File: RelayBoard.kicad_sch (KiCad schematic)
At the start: 148 parts, among them J1 CONN_03-SCREW-5MM, J11 CONN_03-SCREW-5MM, J12 CONN_03-SCREW-5MM, J13 CONN_03-SCREW-5MM, J14 CONN_03-SCREW-5MM, J15 CONN_03-SCREW-5MM, J16 CONN_03-SCREW-5MM, J17 CONN_03-SCREW-5MM, J18 CONN_03-SCREW-5MM, J2 CONN_03-SCREW-5MM, J22 Conn_01x04, J24 Conn_01x06, J3 CONN_03-SCREW-5MM, J4 CONN_03-SCREW-5MM, J5 CONN_03-SCREW-5MM, J6 CONN_03-SCREW-5MM, J7 CONN_03-SCREW-5MM, J8 CONN_03-SCREW-5MM, K1 SANYOU_SRD_Form_C, K11 SANYOU_SRD_Form_C, K12 SANYOU_SRD_Form_C, K13 SANYOU_SRD_Form_C, K14 SANYOU_SRD_Form_C, K15 SANYOU_SRD_Form_C, K16 SANYOU_SRD_Form_C, K17 SANYOU_SRD_Form_C, K18 SANYOU_SRD_Form_C, K2 SANYOU_SRD_Form_C, K3 SANYOU_SRD_Form_C, K4 SANYOU_SRD_Form_C, K5 SANYOU_SRD_Form_C, K6 SANYOU_SRD_Form_C, K7 SANYOU_SRD_Form_C, K8 SANYOU_SRD_Form_C, Q1 ULN2803ADWR, Q2 ULN2803ADWR, U1 AP1117-33, U3 LTV-847, U4 LTV-847, U5 LTV-847, U6 LTV-847

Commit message: basic design with solid state relays complete
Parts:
- removed D11, D111, D112, D113, D114, D115, D116, D117, D118, D12, D13, D14, D15, D16, D17, D18: 1N4148W, Diode_SMD:D_SOD-123, symbol Diode:1N4148W
- removed K1, K11, K12, K13, K14, K15, K16, K17, K18, K2, K3, K4, K5, K6, K7, K8: SANYOU_SRD_Form_C, Relay_THT:Relay_SPDT_SANYOU_SRD_Series_Form_C, symbol Relay:SANYOU_SRD_Form_C
- removed R12, R13, R14, R15, R16, R17, R18, R19, R20, R21, R22, R23, R24, R25, R26, R27: 150, Resistor_SMD:R_0402_1005Metric, symbol Device:R
- removed U3, U4, U5, U6: LTV-847, digikey-footprints:DIP-16_W7.62mm, symbol dk_Optoisolators-Transistor-Photovoltaic-Output:LTV-847
- added U1, U11, U12, U13, U14, U15, U16, U17, U18, U2, U3, U4, U5, U6, U7, U8: (no value), symbol Relay_SolidState:TLP148G
- UP1: renamed from U1; value AP1117-33 -> (none); footprint Package_TO_SOT_SMD:SOT-223-3_TabPin2 -> (none)
- renumbered U2 to UM2
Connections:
- net LED1: now also UM2.5 (GPIO36)
- net LED2: now also UM2.8 (GPIO39)
- net LED3: now also UM2.10 (GPIO34)
- net LED4: now also UM2.11 (GPIO35)
- net at J1.3: now also U1.4
- net at D31.2 (A): now also U1.3
- net at J1.2: now also U1.5
- net at J1.1: now also U1.6
- net at R101.1: now also Q1.18 (OUT1), U1.1
- net at J11.1: now also U11.6
- net at J11.2: now also U11.5
- net at J11.3: now also U11.4
- net at D34.2 (A): now also U4.3
- net at R115.1: now also Q2.14 (OUT5), U15.1
- net at R114.1: now also Q2.15 (OUT4), U14.1
- net at R107.1: now also Q1.12 (OUT7), U7.1
- net at R104.1: now also Q1.16 (OUT3), U4.1
- net at R103.1: now also Q1.15 (OUT4), U3.1
- net at D37.2 (A): now also U7.3
- net at D32.2 (A): now also U2.3
- net at D315.2 (A): now also U15.3
- net at R117.1: now also Q2.12 (OUT7), U17.1
- net at D38.2 (A): now also U8.3
- net at J2.1: now also U2.6
- net at J2.2: now also U2.5
- net at J2.3: now also U2.4
- net at R112.1: now also Q2.17 (OUT2), U12.1
- net at Q2.11 (OUT8): now also R118.1, U18.1
- net at Q2.13 (OUT6): now also R116.1, U16.1
- net at Q2.16 (OUT3): now also R113.1, U13.1
- net at Q2.18 (OUT1): now also R111.1, U11.1
- net at D35.2 (A): now also U5.3
- net at D36.2 (A): now also U6.3
- net at R108.1: now also Q1.11 (OUT8), U8.1
- net at R102.1: now also Q1.17 (OUT2), U2.1
- net at R105.1: now also Q1.14 (OUT5), U5.1
- net at J17.3: now also U17.4
- net at D317.2 (A): now also U17.3
- net at J17.2: now also U17.5
- net at J17.1: now also U17.6
- net at R106.1: now also Q1.13 (OUT6), U6.1
- net at J4.3: now also U4.4
- net at J4.2: now also U4.5
- net at J4.1: now also U4.6
- net at J14.1: now also U14.6
- net at J14.2: now also U14.5
- net at J14.3: now also U14.4
- net at D314.2 (A): now also U14.3
- net at J12.1: now also U12.6
- net at J12.2: now also U12.5
- net at J12.3: now also U12.4
- net at D312.2 (A): now also U12.3
- net at D311.2 (A): now also U11.3
- net at J3.1: now also U3.6
- net at J3.2: now also U3.5
- net at J3.3: now also U3.4
- net at J5.3: now also U5.4
- net at J5.2: now also U5.5
- net at J5.1: now also U5.6
- net at J6.3: now also U6.4
- net at J6.2: now also U6.5
- net at J6.1: now also U6.6
- net at J13.1: now also U13.6
- net at J13.2: now also U13.5
- net at J13.3: now also U13.4
- net at D313.2 (A): now also U13.3
- net at J15.1: now also U15.6
- net at J15.2: now also U15.5
- net at J15.3: now also U15.4
- net at J18.1: now also U18.6
- net at J18.2: now also U18.5
- net at J18.3: now also U18.4
- net at J8.1: now also U8.6
- net at J8.2: now also U8.5
- net at J8.3: now also U8.4
- net at D33.2 (A): now also U3.3
- net at D316.2 (A): now also U16.3
- net at J7.1: now also U7.6
- net at J7.2: now also U7.5
- net at J7.3: now also U7.4
- net at J16.1: now also U16.6
- net at J16.2: now also U16.5
- net at J16.3: now also U16.4
- net at D318.2 (A): now also U18.3

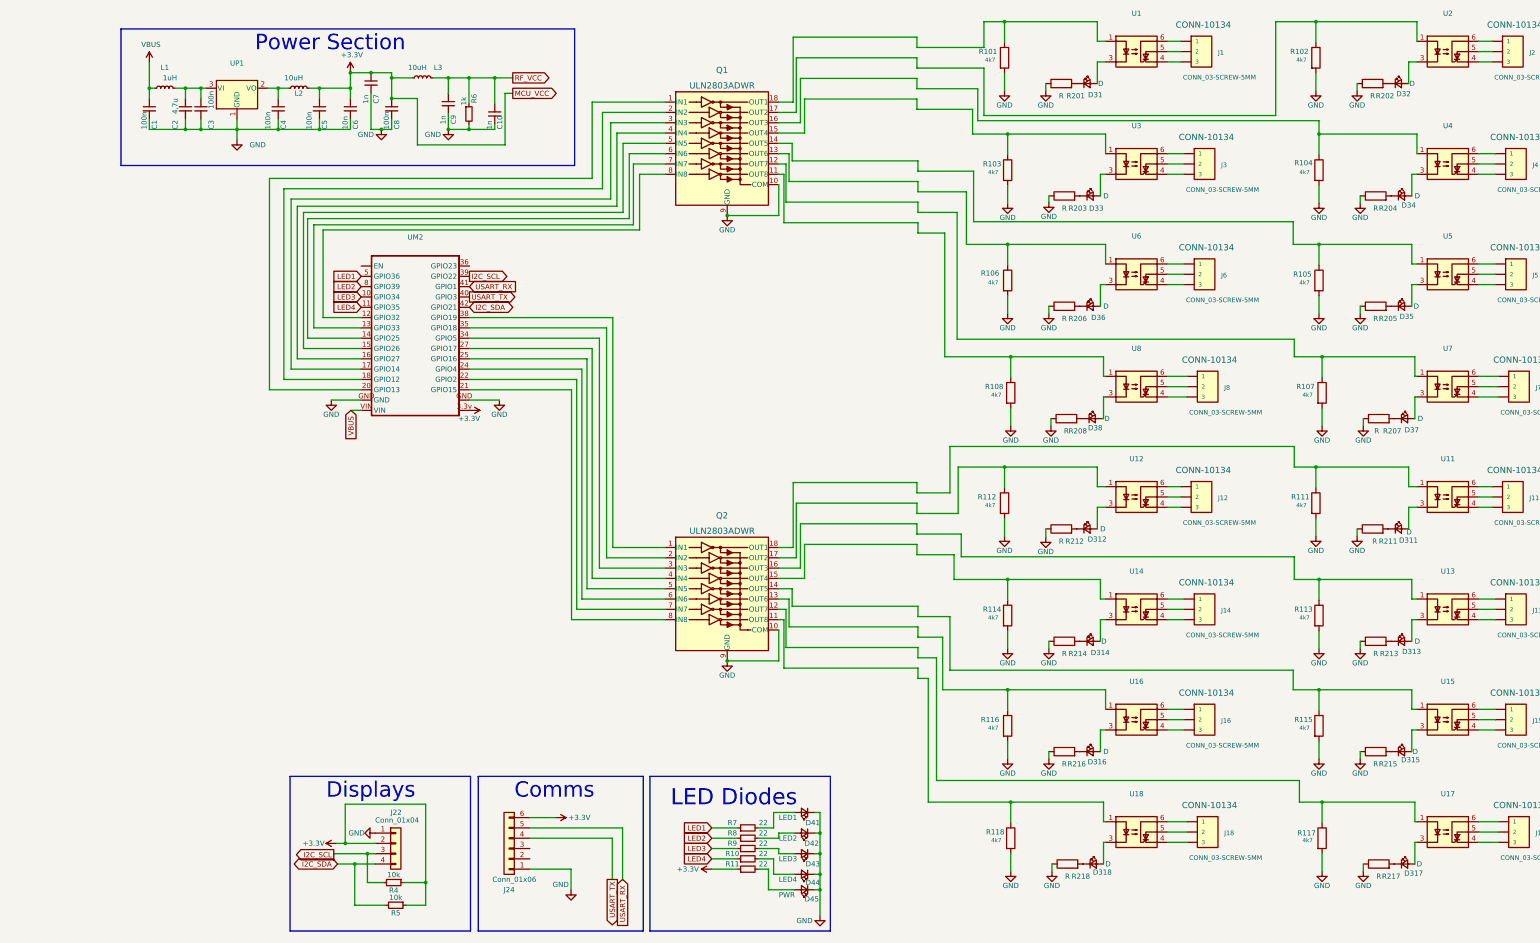
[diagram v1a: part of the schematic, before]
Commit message: remove esp32 and add Raspberry PI, along with AC power suppply
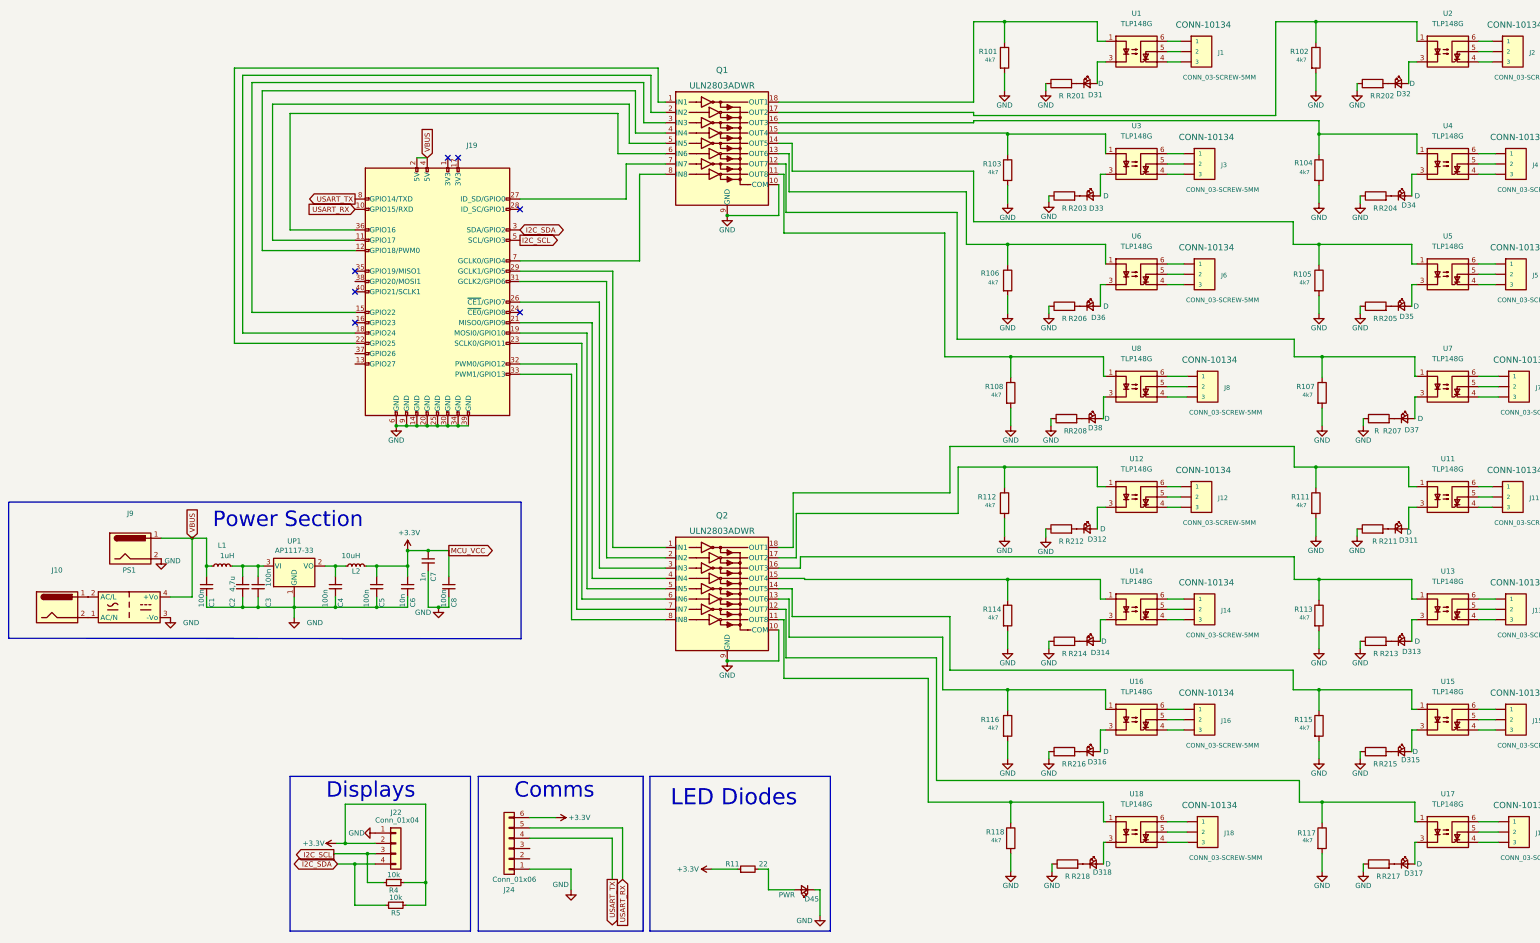
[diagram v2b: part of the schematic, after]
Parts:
- removed C10, C9: 1n, Capacitor_SMD:C_0603_1608Metric, symbol Device:C_Small
- removed D41: LED1, LED_SMD:LED_0402_1005Metric, symbol Device:LED_Small
- removed D42: LED2, LED_SMD:LED_0402_1005Metric, symbol Device:LED_Small
- removed D43: LED3, LED_SMD:LED_0402_1005Metric, symbol Device:LED_Small
- removed D44: LED4, LED_SMD:LED_0402_1005Metric, symbol Device:LED_Small
- removed L3: 10uH, Inductor_SMD:L_0805_2012Metric, symbol Device:L_Small
- removed R10, R7, R8, R9: 22, Resistor_SMD:R_0402_1005Metric, symbol Device:R_Small
- removed R6: 1k, Resistor_SMD:R_0805_2012Metric, symbol Device:R_Small
- removed UM2: (no value), symbol MCU_Espressif:NodeMCUDevKitV1
- added J10, J9: (no value), Connector_BarrelJack:BarrelJack_SwitchcraftConxall_RAPC10U_Horizontal, symbol Connector:Barrel_Jack
- added J19: (no value), symbol Connector:Raspberry_Pi_2_3
- added PS1: (no value), symbol Converter_ACDC:IRM-02-5
- U1, U11, U12, U13, U14, U15, U16, U17, U18, U2, U3, U4, U5, U6, U7, U8: value (none) -> TLP148G; footprint (none) -> Package_SO:MFSOP6-5_4.4x3.6mm_P1.27mm
- UP1: value (none) -> AP1117-33; footprint (none) -> Package_TO_SOT_SMD:SOT-223-3_TabPin2
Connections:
- net GND: now also J19.14 (GND), J19.20 (GND), J19.25 (GND), J19.30 (GND), J19.34 (GND), J19.39 (GND), J19.6 (GND), J19.9 (GND), J9.2, PS1.3 (-Vo)
- net I2C_SCL: now also J19.5 (SCL/GPIO3)
- net I2C_SDA: now also J19.3 (SDA/GPIO2)
- net USART_RX: now also J19.10 (GPIO15/RXD)
- net USART_TX: now also J19.8 (GPIO14/TXD)
- net VBUS: now also J19.2 (5V), J19.4 (5V), J9.1, PS1.4 (+Vo)
- net at Q2.1 (IN1): now also J19.29 (GCLK1/GPIO5)
- net at Q2.2 (IN2): now also J19.31 (GCLK2/GPIO6)
- net at Q2.3 (IN3): now also J19.26 (~{CE1}/GPIO7)
- net at Q2.4 (IN4): now also J19.21 (MISO0/GPIO9)
- net at Q2.5 (IN5): now also J19.19 (MOSI0/GPIO10)
- net at Q2.6 (IN6): now also J19.23 (SCLK0/GPIO11)
- net at Q2.7 (IN7): now also J19.32 (PWM0/GPIO12)
- net at Q2.8 (IN8): now also J19.33 (PWM1/GPIO13)
- net at Q1.8 (IN8): now also J19.7 (GCLK0/GPIO4)
- net at Q1.7 (IN7): now also J19.27 (ID_SD/GPIO0)
- net at Q1.6 (IN6): now also J19.36 (GPIO16)
- net at Q1.5 (IN5): now also J19.11 (GPIO17)
- net at Q1.4 (IN4): now also J19.12 (GPIO18/PWM0)
- net at Q1.3 (IN3): now also J19.15 (GPIO22)
- net at Q1.2 (IN2): now also J19.18 (GPIO24)
- net at Q1.1 (IN1): now also J19.22 (GPIO25)
- new net: J10.1, PS1.2 (AC/L)
- new net: J10.2, PS1.1 (AC/N)
- no-connect marks 0 -> 7
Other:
- moved on the sheet: C1, C2, C3, C4, C5, C6, C7, C8, L1, L2, UP1

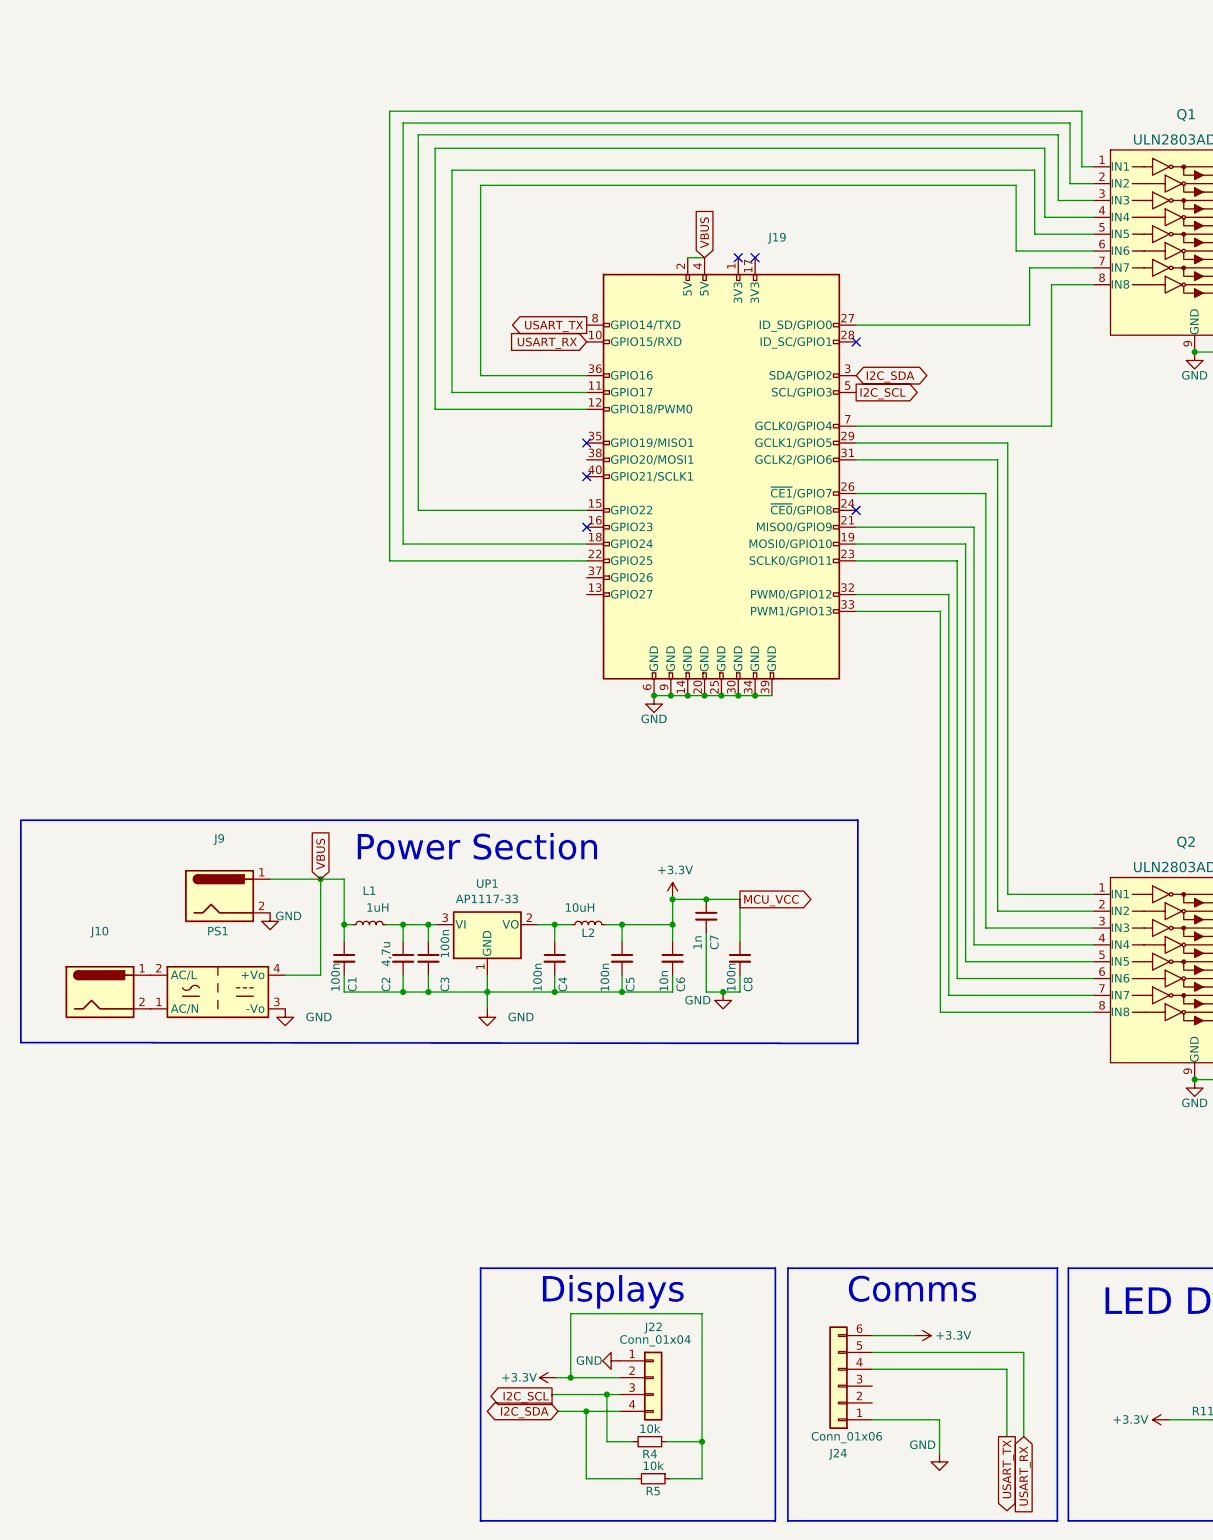
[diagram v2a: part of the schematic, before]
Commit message: replace connectors, reroute GPIOs and power
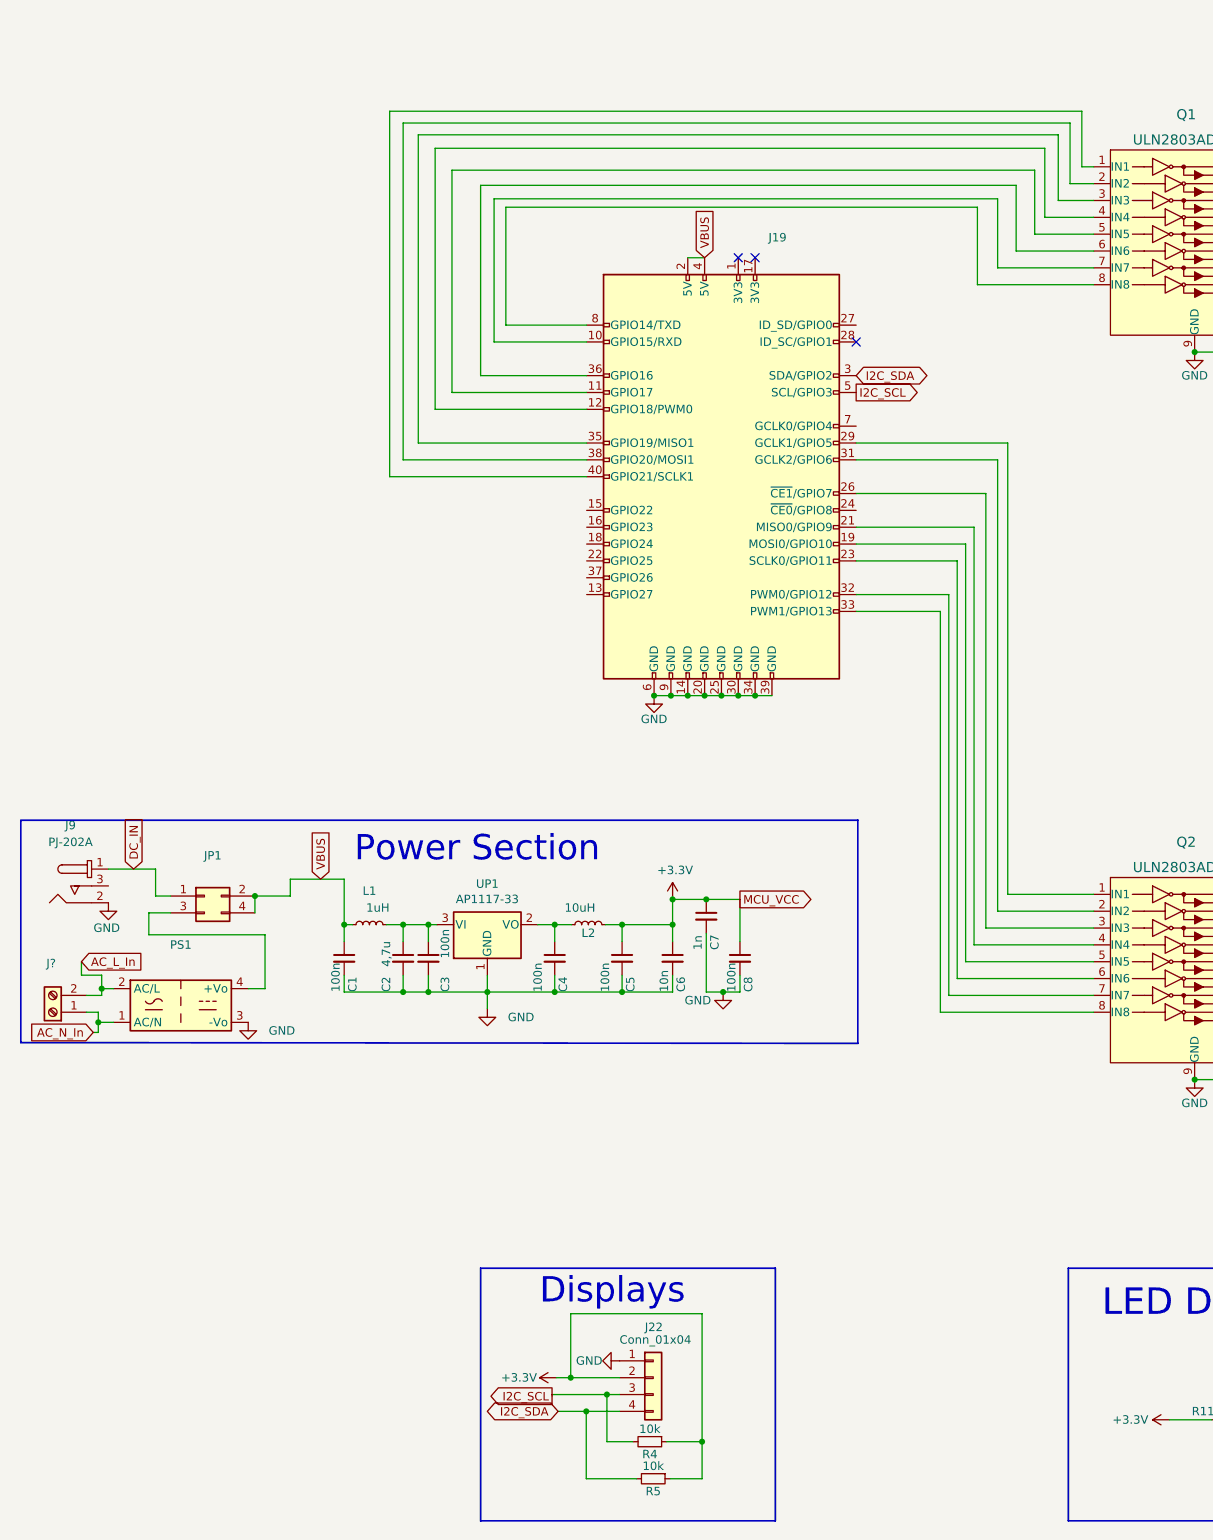
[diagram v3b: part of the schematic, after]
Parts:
- removed J10, J9: (no value), Connector_BarrelJack:BarrelJack_SwitchcraftConxall_RAPC10U_Horizontal, symbol Connector:Barrel_Jack
- removed J24: Conn_01x06, Connector_PinHeader_1.27mm:PinHeader_1x06_P1.27mm_Vertical, symbol Connector_Generic:Conn_01x06
- added J9: PJ-202A, Connectors:POWER_JACK_PTH_LOCK, symbol dk_Barrel-Power-Connectors:PJ-202A
- added J?: (no value), symbol Connector:Screw_Terminal_01x02
- added JP1: (no value), symbol Connector_Generic:Conn_02x02_Odd_Even
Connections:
- net USART_RX is gone; now on an unnamed net: J19.10 (GPIO15/RXD)
- net GND: now also J9.2
- net VBUS: now also JP1.2 (Pin_2), JP1.4 (Pin_4); no longer PS1.4 (+Vo)
- net at J19.15 (GPIO22): no longer Q1.3 (IN3)
- net at J19.18 (GPIO24): no longer Q1.2 (IN2)
- net at J19.22 (GPIO25): no longer Q1.1 (IN1)
- net at Q1.7 (IN7): no longer J19.27 (ID_SD/GPIO0)
- net at J19.35 (GPIO19/MISO1): now also Q1.3 (IN3)
- net at J19.38 (GPIO20/MOSI1): now also Q1.2 (IN2)
- net at J19.40 (GPIO21/SCLK1): now also Q1.1 (IN1)
- net at J19.7 (GCLK0/GPIO4): no longer Q1.8 (IN8)
- net AC_L_In: now reaches PS1.2 (AC/L)
- net AC_L_In: now also J?.2 (Pin_2)
- net AC_N_In: now reaches PS1.1 (AC/N)
- net AC_N_In: now also J?.1 (Pin_1)
- net USART_TX: no longer names the net of J19.8 (GPIO14/TXD)
- net USART_TX: now also Q1.8 (IN8)
- new net: JP1.3 (Pin_3), PS1.4 (+Vo)
- new net DC_IN: J9.1, JP1.1 (Pin_1)
- no-connect marks 7 -> 3
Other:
- note removed: "Comms"
- moved on the sheet: PS1
